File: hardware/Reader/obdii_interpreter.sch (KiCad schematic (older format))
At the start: 2 parts

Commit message: Fixed numerous bugs in design for Reader Schematic and PCB
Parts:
- J_OBD_2: Part Name (none) -> 4157
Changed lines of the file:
@@
 F 5 "Adafruit Industries LLC" H 5650 7500 50  0001 C CNN "Manufacturer"
 F 6 "1528-2929-ND" H 5650 7500 50  0001 C CNN "digikeypn"
+F 7 "4157" H 5650 7500 50  0001 C CNN "Part Name"
 	1    5650 7500
 	0    1    1    0

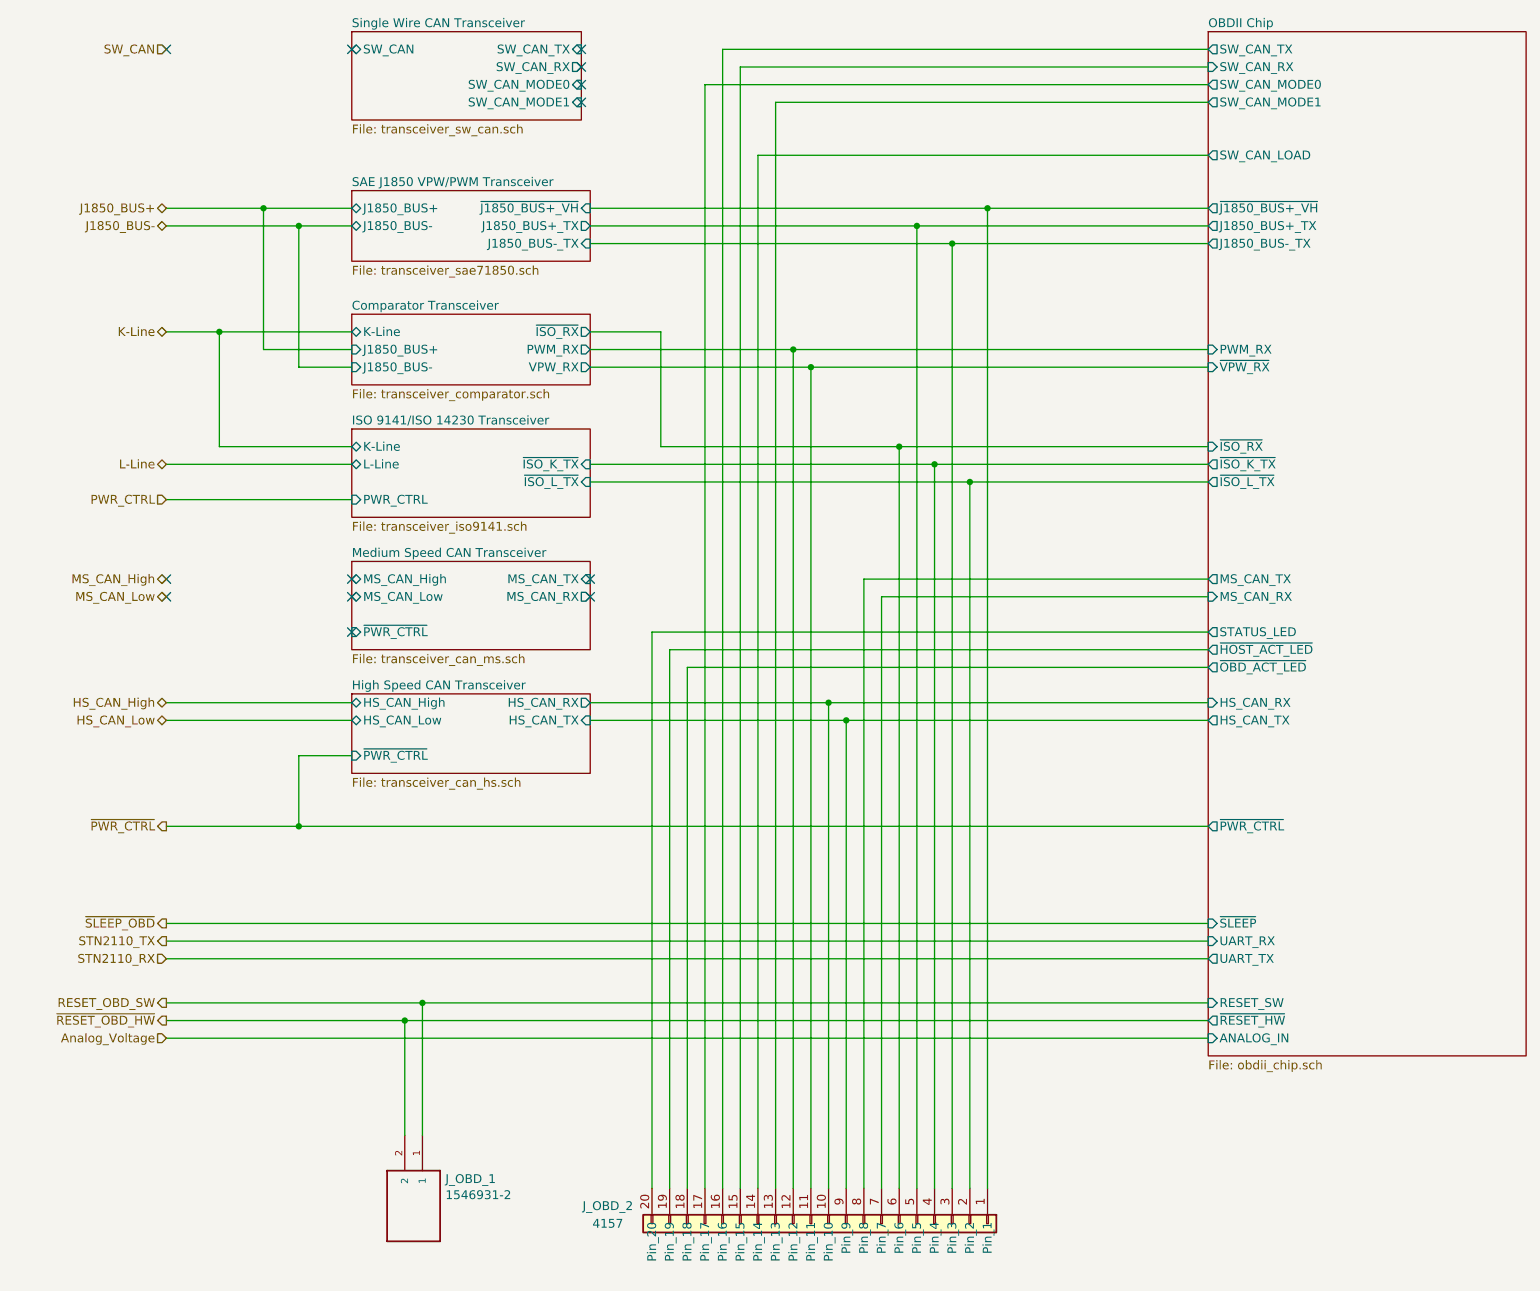
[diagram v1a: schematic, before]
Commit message: Updated reader schematic to v0.0.5 by adding ESP32, removing unused transceivers, fixed design flaws, increased header pins and fixed footprints. Working on reader PCB design
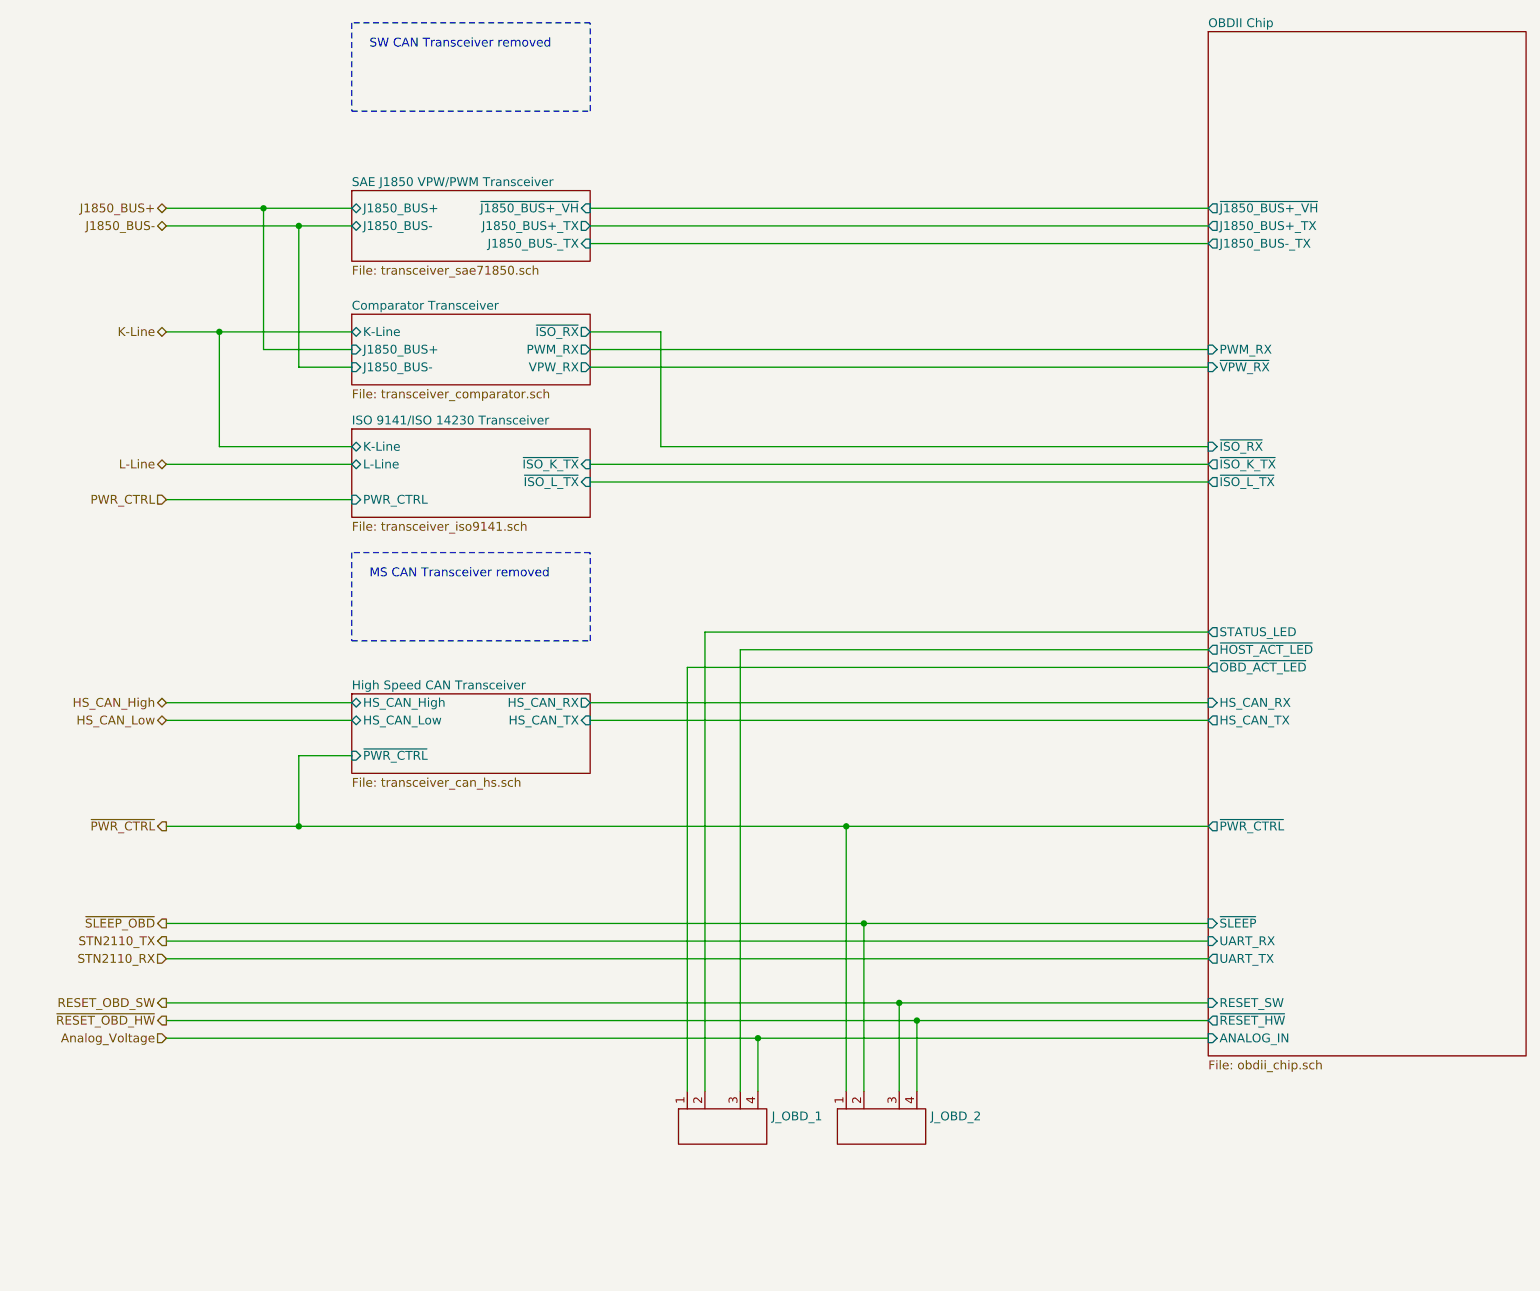
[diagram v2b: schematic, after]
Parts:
- removed J_OBD_1: 1546931-2, footprints:1546931-2, symbol 1546931-2:1546931-2
- removed J_OBD_2: 4157, Connector_PinSocket_2.54mm:PinSocket_1x20_P2.54mm_Vertical, symbol CANtech:4157
- added J_OBD_1, J_OBD_2: Header_Pin_4, Connector_PinHeader_2.54mm:PinHeader_1x04_P2.54mm_Vertical, symbol CANtech:Header_Pin_4
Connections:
- net Analog_Voltage: now also J_OBD_1.4
- net OBDII Chip/STATUS_LED: now also J_OBD_1.2
- net OBDII Chip/~HOST_ACT_LED~: now also J_OBD_1.3
- net OBDII Chip/~OBD_ACT_LED~: now also J_OBD_1.1
- net RESET_OBD_SW: now also J_OBD_2.3
- net ~PWR_CTRL~: now also J_OBD_2.1
- net ~RESET_OBD_HW~: now also J_OBD_2.4
- net ~SLEEP_OBD~: now also J_OBD_2.2
- no-connect marks 13 -> 0
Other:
- note added: "MS CAN Transceiver removed"
- note added: "SW CAN Transceiver removed"

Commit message: Updated schematic and gerber to v0.0.05. Added ESP32. Removed MS CAN and SW CAN Transceivers. Added silkscreen text to header pins. Improved readability
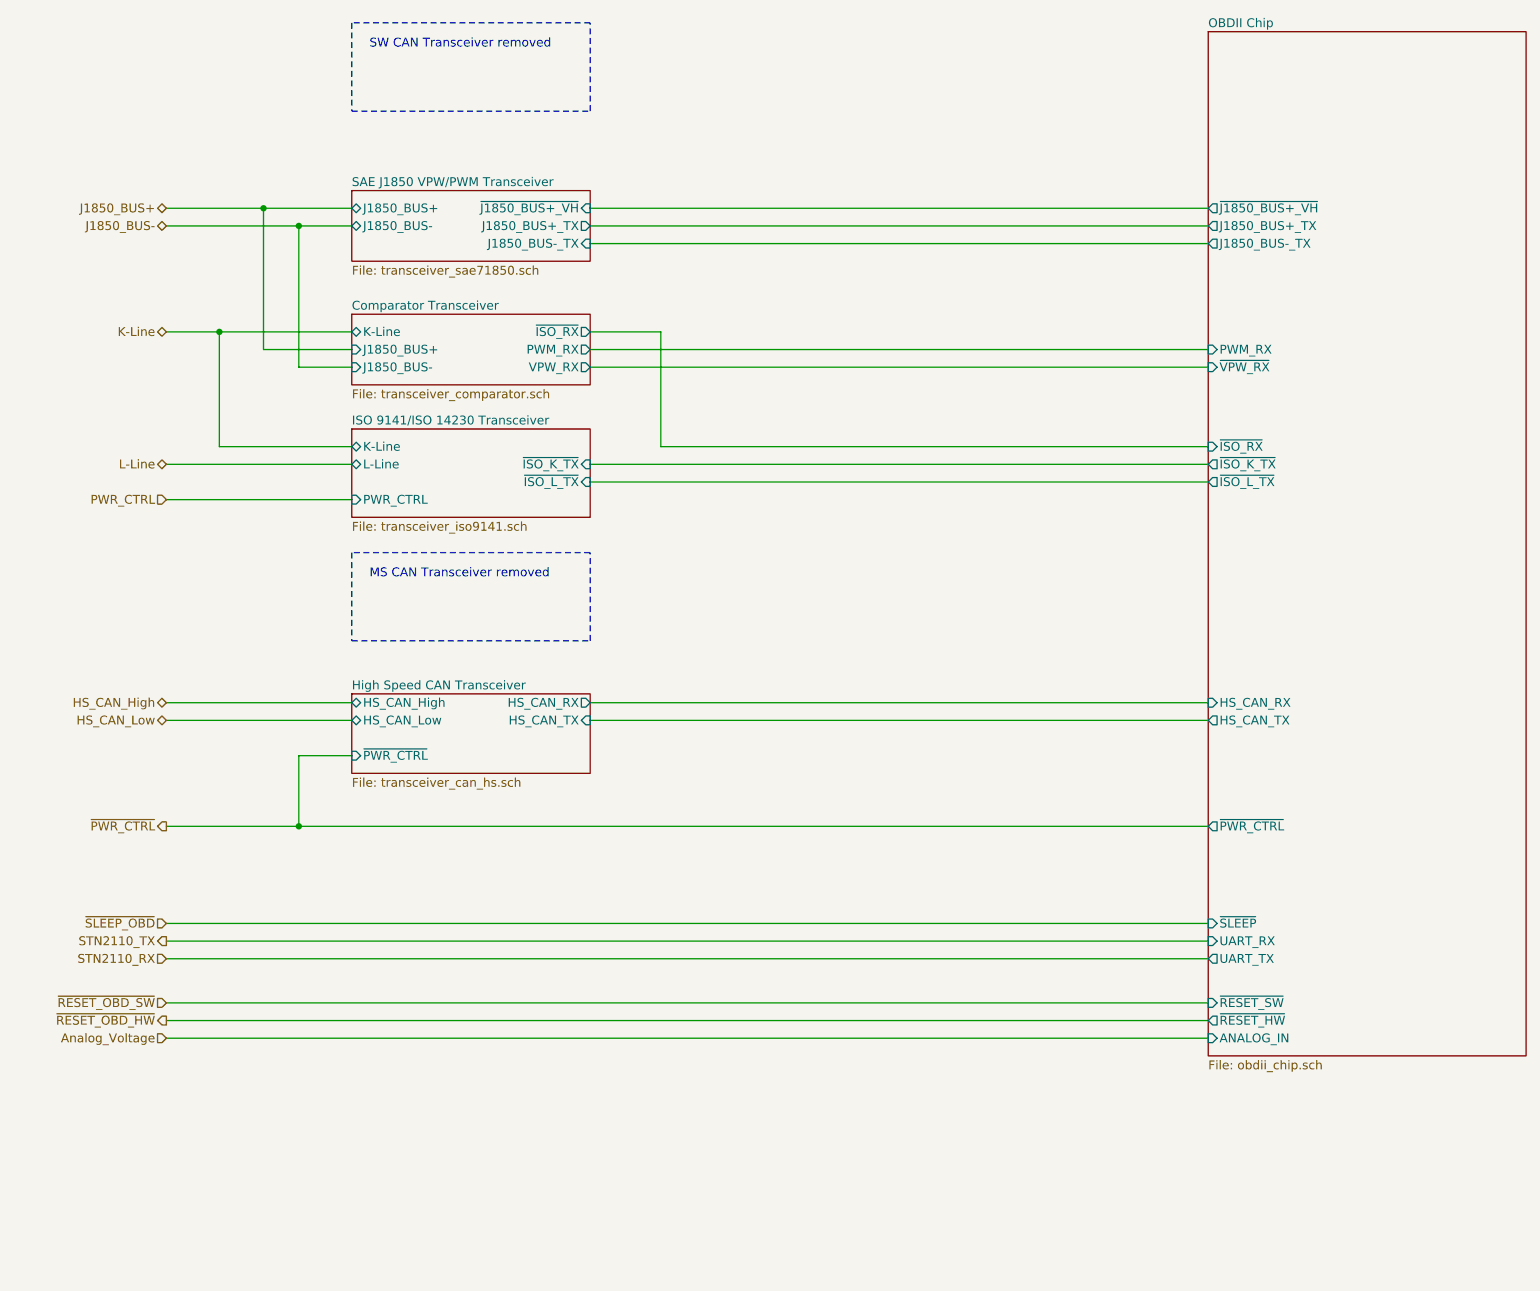
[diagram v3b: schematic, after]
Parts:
- removed J_OBD_1, J_OBD_2: Header_Pin_4, Connector_PinHeader_2.54mm:PinHeader_1x04_P2.54mm_Vertical, symbol CANtech:Header_Pin_4
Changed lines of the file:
@@
 Sheet 12 17
 Title "CANnect Reader | OBD-II Interpreter"
-Date "2020-11-27"
+Date "2020-11-29"
 Rev "0.0.05"
 Comp "CANtech"
@@
 Wire Wire Line
 	2150 4900 2150 5300
-Text HLabel 1400 5850 0    50   Output ~ 0
+Text HLabel 1400 5850 0    50   Input ~ 0
 ~SLEEP_OBD~
 Text HLabel 1400 3450 0    50   Input ~ 0
@@
 Wire Wire Line
 	4200 2500 4200 3150
-Wire Wire Line
-	7300 4400 4350 4400
 Wire Wire Line
 	1400 5950 7300 5950
@@
 F4 "HS_CAN_TX" O L 7300 4700 50
 F5 "HS_CAN_RX" I L 7300 4600 50
-F6 "~OBD_ACT_LED~" O L 7300 4400 50
-F7 "~RESET_HW~" O L 7300 6400 50
-F8 "~HOST_ACT_LED~" O L 7300 4300 50
-F9 "STATUS_LED" O L 7300 4200 50
-F10 "RESET_SW" I L 7300 6300 50
-F11 "ANALOG_IN" I L 7300 6500 50
-F12 "~ISO_RX~" I L 7300 3150 50
-F13 "~VPW_RX~" I L 7300 2700 50
-F14 "~SLEEP~" I L 7300 5850 50
-F15 "PWM_RX" I L 7300 2600 50
-F16 "J1850_BUS+_TX" O L 7300 1900 50
-F17 "~J1850_BUS+_VH~" O L 7300 1800 50
-F18 "J1850_BUS-_TX" O L 7300 2000 50
-F19 "~PWR_CTRL~" O L 7300 5300 50
-F20 "~ISO_L_TX~" O L 7300 3350 50
-F21 "~ISO_K_TX~" O L 7300 3250 50
-$EndSheet
-Wire Wire Line
-	1400 6500 4750 6500
+F6 "~RESET_HW~" O L 7300 6400 50
+F7 "ANALOG_IN" I L 7300 6500 50
+F8 "~ISO_RX~" I L 7300 3150 50
+F9 "~VPW_RX~" I L 7300 2700 50
+F10 "~SLEEP~" I L 7300 5850 50
+F11 "PWM_RX" I L 7300 2600 50
+F12 "J1850_BUS+_TX" O L 7300 1900 50
+F13 "~J1850_BUS+_VH~" O L 7300 1800 50
+F14 "J1850_BUS-_TX" O L 7300 2000 50
+F15 "~PWR_CTRL~" O L 7300 5300 50
+F16 "~ISO_L_TX~" O L 7300 3350 50
+F17 "~ISO_K_TX~" O L 7300 3250 50
+F18 "~RESET_SW~" I L 7300 6300 50
+$EndSheet
 Text HLabel 1400 6400 0    50   Output ~ 0
 ~RESET_OBD_HW~
-Text HLabel 1400 6300 0    50   Output ~ 0
-RESET_OBD_SW
+Text HLabel 1400 6300 0    50   Input ~ 0
+~RESET_OBD_SW~
 Text HLabel 1400 6500 0    50   Input ~ 0
 Analog_Voltage
@@
 Wire Wire Line
 	3800 1800 7300 1800
-$Comp
-L CANtech:Header_Pin_4 J_OBD_2
-U 1 1 5FCDCC00
-P 5450 6750
-F 0 "J_OBD_2" H 5728 6558 50  0000 L CNN
-F 1 "Header_Pin_4" H 5450 6750 50  0001 C CNN
-F 2 "Connector_PinHeader_2.54mm:PinHeader_1x04_P2.54mm_Vertical" H 5450 6750 50  0001 C CNN
-F 3 "" H 5450 6750 50  0001 C CNN
-	1    5450 6750
-	1    0    0    -1
-$EndComp
-Wire Wire Line
-	5250 6800 5250 5300
-Wire Wire Line
-	5350 6800 5350 5850
-Wire Wire Line
-	5550 6800 5550 6300
-Wire Wire Line
-	5650 6400 5650 6800
-Connection ~ 5250 5300
-Wire Wire Line
-	5250 5300 7300 5300
-Connection ~ 5350 5850
-Wire Wire Line
-	5350 5850 7300 5850
-Connection ~ 5550 6300
-Wire Wire Line
-	5550 6300 7300 6300
-Connection ~ 5650 6400
-Wire Wire Line
-	5650 6400 7300 6400
-Wire Wire Line
-	1400 5850 5350 5850
-Wire Wire Line
-	2150 5300 5250 5300
-Wire Wire Line
-	1400 6300 5550 6300
-Wire Wire Line
-	1400 6400 5650 6400
-Wire Wire Line
-	4450 4200 7300 4200
-Wire Wire Line
-	4650 4300 7300 4300
-Wire Wire Line
-	4650 4300 4650 6800
-Wire Wire Line
-	4450 6800 4450 4200
-Wire Wire Line
-	4350 6800 4350 4400
-$Comp
-L CANtech:Header_Pin_4 J_OBD_1
-U 1 1 5FCEC5FD
-P 4550 6750
-F 0 "J_OBD_1" H 4828 6558 50  0000 L CNN
-F 1 "Header_Pin_4" H 4550 6750 50  0001 C CNN
-F 2 "Connector_PinHeader_2.54mm:PinHeader_1x04_P2.54mm_Vertical" H 4550 6750 50  0001 C CNN
-F 3 "" H 4550 6750 50  0001 C CNN
-	1    4550 6750
-	1    0    0    -1
-$EndComp
-Wire Wire Line
-	4750 6800 4750 6500
-Connection ~ 4750 6500
-Wire Wire Line
-	4750 6500 7300 6500
 Wire Notes Line
 	2450 750  2450 1250
@@
 Text Notes 2550 3900 0    50   ~ 0
 MS CAN Transceiver removed
+Wire Wire Line
+	1400 6500 7300 6500
+Wire Wire Line
+	2150 5300 7300 5300
+Wire Wire Line
+	1400 5850 7300 5850
+Wire Wire Line
+	1400 6300 7300 6300
+Wire Wire Line
+	1400 6400 7300 6400
 $EndSCHEMATC
